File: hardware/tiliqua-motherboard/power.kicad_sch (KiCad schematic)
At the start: 33 parts, among them J6 CONN 2x5 P=2.54mm, U10 TPS7A91, U5 AP63200WU

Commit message: * bump +12V ingress fuse 350mA/500mA
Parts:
- F1: value 16V 350mA -> 16V 500mA; LCSC C883107 -> C2833485; lcsc# C883107 -> C2833485
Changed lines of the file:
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@@
 			)
 		)
-		(property "Value" "16V 350mA"
+		(property "Value" "16V 500mA"
 			(at 55.88 45.974 90)
 			(effects
@@
 			)
 		)
-		(property "lcsc#" "C883107"
+		(property "lcsc#" "C2833485"
 			(at 55.88 48.26 90)
 			(effects
@@
 			)
 		)
-		(property "LCSC" "C883107"
+		(property "LCSC" "C2833485"
 			(at 55.88 43.942 0)
 			(effects

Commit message: * BOM: update some LCSC fields
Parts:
- R17: LCSC C861679 -> C99856
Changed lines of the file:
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@@
 			)
 		)
-		(property "LCSC" "C861679"
+		(property "LCSC" "C99856"
 			(at 120.65 118.11 0)
 			(effects

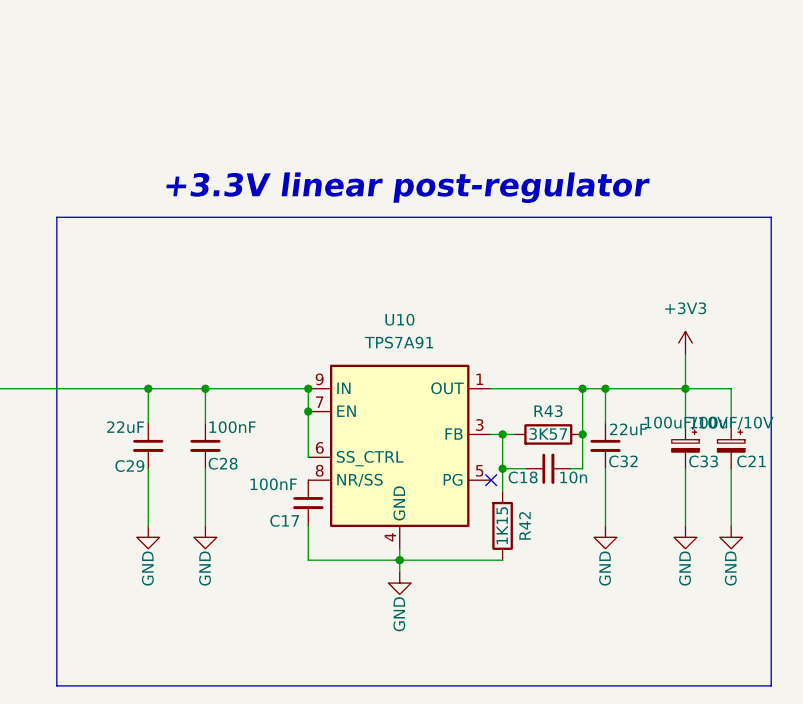
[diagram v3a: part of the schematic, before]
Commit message: * power: swap out 3V3 LDO for SMPS
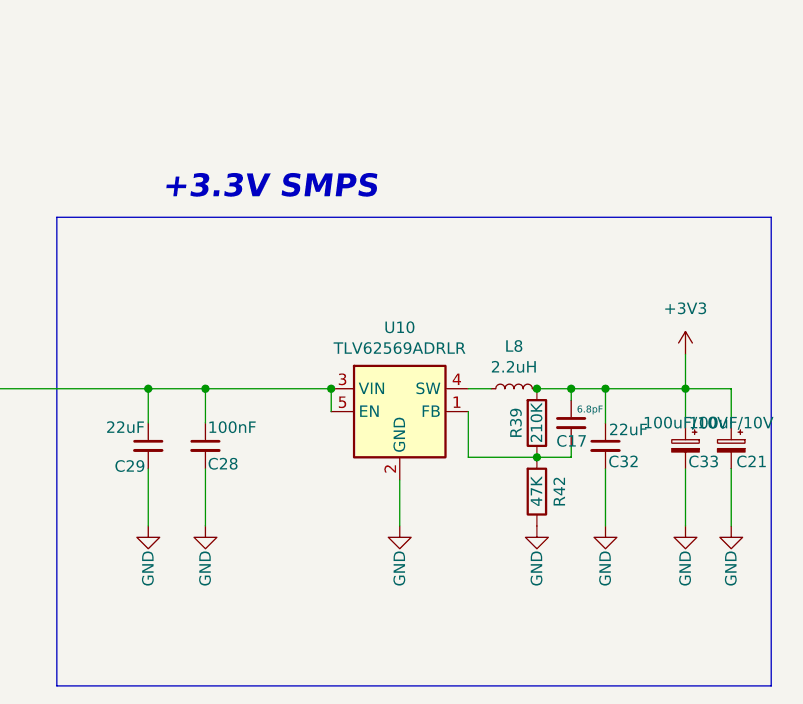
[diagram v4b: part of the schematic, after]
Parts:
- removed C17: 100nF, Capacitor_SMD:C_0402_1005Metric, symbol Device:C_Small
- removed C18: 10n, Capacitor_SMD:C_0402_1005Metric, symbol Device:C_Small
- removed R43: 3K57, Resistor_SMD:R_0402_1005Metric, symbol Device:R
- removed U10: TPS7A91, Package_DFN_QFN:Texas_S-PDSO-N10_EP1.2x2mm_ThermalVias, symbol Regulator_Linear:TPS7A91
- added C17: 6.8pF, Capacitor_SMD:C_0402_1005Metric, symbol OLIMEX_RCL:C
- added L8: 2.2uH, Inductor_SMD:L_0805_2012Metric, symbol Device:L_Small
- added R39: 210K, Resistor_SMD:R_0402_1005Metric, symbol Device:R
- added U10: TLV62569ADRLR, Package_TO_SOT_SMD:SOT-563, symbol Regulator_Switching:TLV62569DRL
- R42: value 1K15 -> 47K; LCSC C29401 -> (none); lcsc# C29401 -> (none)
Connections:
- net +3V3: now also C17.1, L8.2, R39.2
- net GND: now also U10.2 (GND)
- net at C28.1, C29.1, L4.1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: now also U10.3 (VIN), U10.5 (EN)
- net at R42.2: now also C17.2, R39.1, U10.1 (FB)
- new net: L8.1, U10.4 (SW)
- no-connect marks 2 -> 1
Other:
- note added: "+3.3V SMPS"
- note removed: "+3.3V linear post-regulator"
